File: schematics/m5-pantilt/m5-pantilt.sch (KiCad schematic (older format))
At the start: 11 parts, among them J1 Conn_02x15_Odd_Even, J2 Conn_02x03_Odd_Even, J3 Conn_02x03_Odd_Even, J4 Conn_02x03_Odd_Even, J5 BAT, J6 Conn_01x04, SW1 SW_SPDT, U1 NL27WZ125

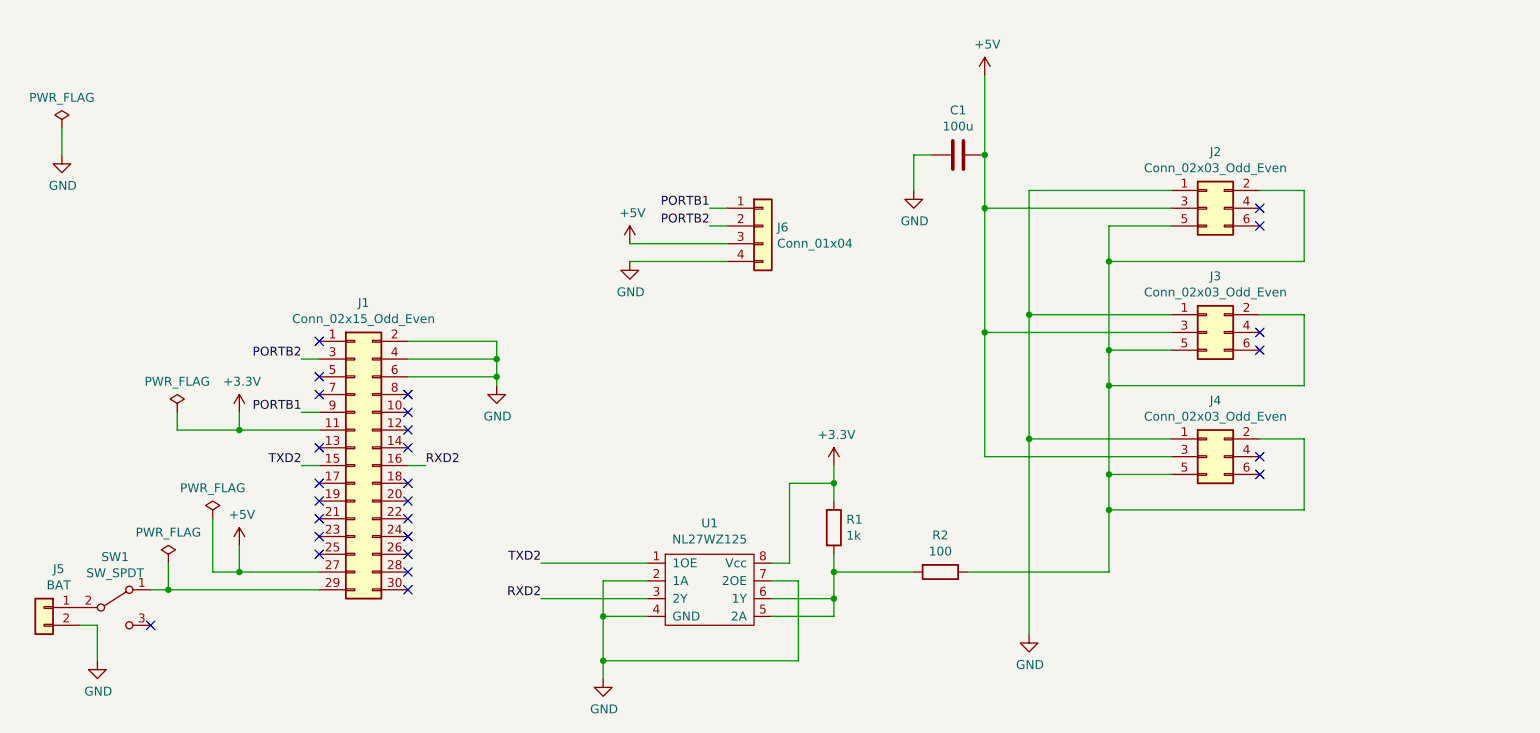
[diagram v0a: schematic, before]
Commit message: Make schematics and layout
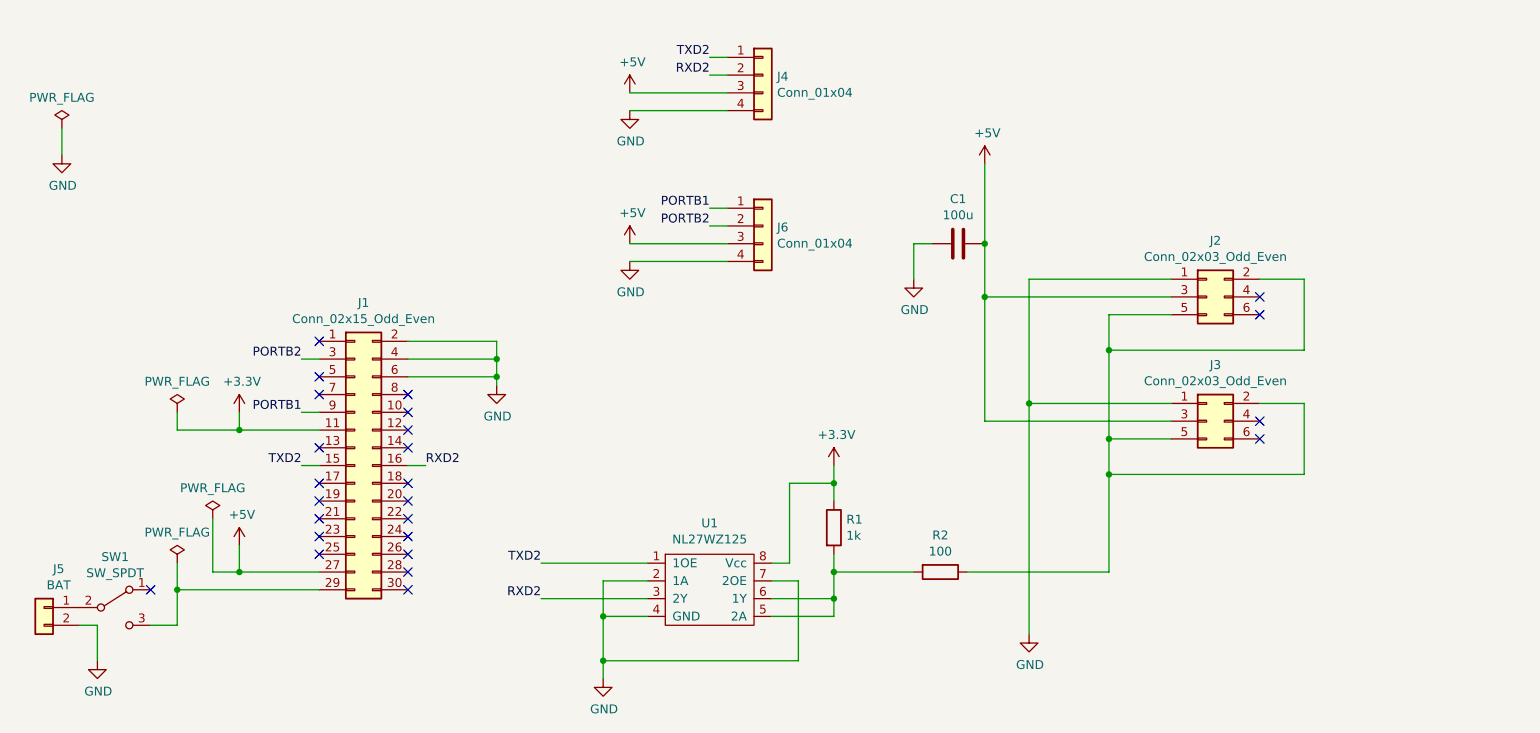
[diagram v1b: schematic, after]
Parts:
- removed J4: Conn_02x03_Odd_Even, Connector_PinHeader_2.54mm:PinHeader_2x03_P2.54mm_Vertical, symbol Connector_Generic:Conn_02x03_Odd_Even
- added J4: Conn_01x04, Connector_JST:JST_PH_S4B-PH-K_1x04_P2.00mm_Horizontal, symbol Connector_Generic:Conn_01x04
- J1: footprint Connector_PinHeader_2.54mm:PinHeader_2x15_P2.54mm_Vertical -> Connector_PinHeader_2.54mm:PinHeader_2x15_P2.54mm_Vertical_SMD
- SW1: footprint Button_Switch_THT:SW_CuK_OS102011MA1QN1_SPDT_Angled -> Button_Switch_THT:SW_E-Switch_EG1224_SPDT_Angled
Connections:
- net +5V: now also J4.3 (Pin_3)
- net GND: now also J4.4 (Pin_4)
- net RXD2: now also J4.2 (Pin_2)
- net TXD2: now also J4.1 (Pin_1)
- net at J1.29 (Pin_29): now also SW1.3 (C); no longer SW1.1 (A)
- no-connect marks 27 -> 25
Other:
- moved on the sheet: C1, J2, J3
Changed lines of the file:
@@
 F 0 "J1" H 3800 5467 50  0000 C CNN
 F 1 "Conn_02x15_Odd_Even" H 3800 5376 50  0000 C CNN
-F 2 "Connector_PinHeader_2.54mm:PinHeader_2x15_P2.54mm_Vertical" H 3750 4550 50  0001 C CNN
+F 2 "Connector_PinHeader_2.54mm:PinHeader_2x15_P2.54mm_Vertical_SMD" H 3750 4550 50  0001 C CNN
 F 3 "~" H 3750 4550 50  0001 C CNN
 	1    3750 4550
@@
 L Connector_Generic:Conn_02x03_Odd_Even J3
 U 1 1 60BD706E
-P 8550 3800
-F 0 "J3" H 8600 4117 50  0000 C CNN
-F 1 "Conn_02x03_Odd_Even" H 8600 4026 50  0000 C CNN
-F 2 "Connector_PinHeader_2.54mm:PinHeader_2x03_P2.54mm_Vertical" H 8550 3800 50  0001 C CNN
-F 3 "~" H 8550 3800 50  0001 C CNN
-	1    8550 3800
-	1    0    0    -1
-$EndComp
-$Comp
-L Connector_Generic:Conn_02x03_Odd_Even J4
-U 1 1 60BD7329
-P 8550 4500
-F 0 "J4" H 8600 4817 50  0000 C CNN
-F 1 "Conn_02x03_Odd_Even" H 8600 4726 50  0000 C CNN
-F 2 "Connector_PinHeader_2.54mm:PinHeader_2x03_P2.54mm_Vertical" H 8550 4500 50  0001 C CNN
-F 3 "~" H 8550 4500 50  0001 C CNN
-	1    8550 4500
+P 8550 4300
+F 0 "J3" H 8600 4617 50  0000 C CNN
+F 1 "Conn_02x03_Odd_Even" H 8600 4526 50  0000 C CNN
+F 2 "Connector_PinHeader_2.54mm:PinHeader_2x03_P2.54mm_Vertical" H 8550 4300 50  0001 C CNN
+F 3 "~" H 8550 4300 50  0001 C CNN
+	1    8550 4300
 	1    0    0    -1
 $EndComp
@@
 L power:+5V #PWR07
 U 1 1 60BFD6E8
-P 7300 2350
-F 0 "#PWR07" H 7300 2200 50  0001 C CNN
-F 1 "+5V" H 7315 2523 50  0000 C CNN
-F 2 "" H 7300 2350 50  0001 C CNN
-F 3 "" H 7300 2350 50  0001 C CNN
-	1    7300 2350
+P 7300 2850
+F 0 "#PWR07" H 7300 2700 50  0001 C CNN
+F 1 "+5V" H 7315 3023 50  0000 C CNN
+F 2 "" H 7300 2850 50  0001 C CNN
+F 3 "" H 7300 2850 50  0001 C CNN
+	1    7300 2850
 	1    0    0    -1
 $EndComp
@@
 	7200 5150 8000 5150
 Wire Wire Line
-	8000 4600 8350 4600
+	8000 4400 8350 4400
+Wire Wire Line
+	8000 4400 8000 4600
+Wire Wire Line
+	8000 4600 9100 4600
+Wire Wire Line
+	9100 4600 9100 4200
+Wire Wire Line
+	9100 4200 8850 4200
 Connection ~ 8000 4600
 Wire Wire Line
-	8000 4600 8000 4800
-Wire Wire Line
-	8000 3900 8350 3900
-Wire Wire Line
-	8000 3900 8000 4100
-Wire Wire Line
-	8000 4100 9100 4100
-Wire Wire Line
-	9100 4100 9100 3700
-Wire Wire Line
-	9100 3700 8850 3700
-Connection ~ 8000 4100
-Wire Wire Line
-	8000 4100 8000 4600
-Wire Wire Line
-	8850 4400 9100 4400
-Wire Wire Line
-	9100 4400 9100 4800
-Wire Wire Line
-	9100 4800 8000 4800
-Connection ~ 8000 4800
-Wire Wire Line
-	8000 4800 8000 5150
-Wire Wire Line
-	7300 3800 8350 3800
-Wire Wire Line
-	7300 2350 7300 2800
-Wire Wire Line
-	7300 3800 7300 4500
-Wire Wire Line
-	7300 4500 8350 4500
-Connection ~ 7300 3800
-NoConn ~ 8850 4500
-NoConn ~ 8850 3800
-NoConn ~ 8850 3900
-NoConn ~ 8850 4600
-Wire Wire Line
-	7550 5500 7550 4400
-Wire Wire Line
-	7550 4400 8350 4400
-Wire Wire Line
-	7550 4400 7550 3700
-Wire Wire Line
-	7550 3700 8350 3700
-Connection ~ 7550 4400
+	7300 4300 8350 4300
+Wire Wire Line
+	7300 2850 7300 3300
+NoConn ~ 8850 4300
+NoConn ~ 8850 4400
+Wire Wire Line
+	7550 4200 8350 4200
 $Comp
 L Connector_Generic:Conn_02x03_Odd_Even J2
 U 1 1 60C1A998
-P 8550 3100
-F 0 "J2" H 8600 3417 50  0000 C CNN
-F 1 "Conn_02x03_Odd_Even" H 8600 3326 50  0000 C CNN
-F 2 "Connector_PinHeader_2.54mm:PinHeader_2x03_P2.54mm_Vertical" H 8550 3100 50  0001 C CNN
-F 3 "~" H 8550 3100 50  0001 C CNN
-	1    8550 3100
-	1    0    0    -1
-$EndComp
-Wire Wire Line
-	8000 3200 8350 3200
-Wire Wire Line
-	8000 3400 9100 3400
-Wire Wire Line
-	7300 3100 8350 3100
-Wire Wire Line
-	7550 3000 8350 3000
-Wire Wire Line
-	8850 3000 9100 3000
-Wire Wire Line
-	9100 3000 9100 3400
-NoConn ~ 8850 3100
-NoConn ~ 8850 3200
-Wire Wire Line
-	8000 3200 8000 3400
-Wire Wire Line
-	8000 3400 8000 3900
-Connection ~ 8000 3400
+P 8550 3600
+F 0 "J2" H 8600 3917 50  0000 C CNN
+F 1 "Conn_02x03_Odd_Even" H 8600 3826 50  0000 C CNN
+F 2 "Connector_PinHeader_2.54mm:PinHeader_2x03_P2.54mm_Vertical" H 8550 3600 50  0001 C CNN
+F 3 "~" H 8550 3600 50  0001 C CNN
+	1    8550 3600
+	1    0    0    -1
+$EndComp
+Wire Wire Line
+	8000 3700 8350 3700
+Wire Wire Line
+	8000 3900 9100 3900
+Wire Wire Line
+	7300 3600 8350 3600
+Wire Wire Line
+	7550 3500 8350 3500
+Wire Wire Line
+	8850 3500 9100 3500
+Wire Wire Line
+	9100 3500 9100 3900
+NoConn ~ 8850 3600
+NoConn ~ 8850 3700
+Wire Wire Line
+	8000 3700 8000 3900
+Wire Wire Line
+	8000 3900 8000 4400
 Connection ~ 8000 3900
-Connection ~ 7300 3100
-Wire Wire Line
-	7300 3100 7300 3800
-Wire Wire Line
-	7550 3000 7550 3700
-Connection ~ 7550 3700
+Connection ~ 8000 4400
+Connection ~ 7300 3600
+Wire Wire Line
+	7300 3600 7300 4300
+Wire Wire Line
+	7550 3500 7550 4200
+Connection ~ 7550 4200
 Text Label 3450 3950 2    50   ~ 0
 PORTB2
@@
 L power:PWR_FLAG #FLG0101
 U 1 1 60C7066B
-P 2700 5100
-F 0 "#FLG0101" H 2700 5175 50  0001 C CNN
-F 1 "PWR_FLAG" H 2700 5273 50  0000 C CNN
-F 2 "" H 2700 5100 50  0001 C CNN
-F 3 "~" H 2700 5100 50  0001 C CNN
-	1    2700 5100
+P 2750 5100
+F 0 "#FLG0101" H 2750 5175 50  0001 C CNN
+F 1 "PWR_FLAG" H 2750 5273 50  0000 C CNN
+F 2 "" H 2750 5100 50  0001 C CNN
+F 3 "~" H 2750 5100 50  0001 C CNN
+	1    2750 5100
 	1    0    0    -1
 $EndComp
@@
 Wire Wire Line
 	5300 3400 5850 3400
-Connection ~ 7300 2800
-Wire Wire Line
-	7300 2800 7300 3100
+Connection ~ 7300 3300
+Wire Wire Line
+	7300 3300 7300 3600
 $Comp
 L power:GND #PWR0101
 U 1 1 60CBA560
-P 6900 3000
-F 0 "#PWR0101" H 6900 2750 50  0001 C CNN
-F 1 "GND" H 6905 2827 50  0000 C CNN
-F 2 "" H 6900 3000 50  0001 C CNN
-F 3 "" H 6900 3000 50  0001 C CNN
-	1    6900 3000
-	1    0    0    -1
-$EndComp
-Wire Wire Line
-	6900 3000 6900 2800
-Wire Wire Line
-	6900 2800 7000 2800
+P 6900 3500
+F 0 "#PWR0101" H 6900 3250 50  0001 C CNN
+F 1 "GND" H 6905 3327 50  0000 C CNN
+F 2 "" H 6900 3500 50  0001 C CNN
+F 3 "" H 6900 3500 50  0001 C CNN
+	1    6900 3500
+	1    0    0    -1
+$EndComp
+Wire Wire Line
+	6900 3500 6900 3300
+Wire Wire Line
+	6900 3300 7000 3300
 $Comp
 L Device:C C1
 U 1 1 60CB98BD
-P 7150 2800
-F 0 "C1" V 7402 2800 50  0000 C CNN
-F 1 "100u" V 7311 2800 50  0000 C CNN
-F 2 "Capacitor_THT:C_Radial_D6.3mm_H11.0mm_P2.50mm" H 7188 2650 50  0001 C CNN
-F 3 "~" H 7150 2800 50  0001 C CNN
-	1    7150 2800
+P 7150 3300
+F 0 "C1" V 7402 3300 50  0000 C CNN
+F 1 "100u" V 7311 3300 50  0000 C CNN
+F 2 "Capacitor_THT:C_Radial_D6.3mm_H11.0mm_P2.50mm" H 7188 3150 50  0001 C CNN
+F 3 "~" H 7150 3300 50  0001 C CNN
+	1    7150 3300
 	0    -1   -1   0
 $EndComp
@@
 F 0 "SW1" H 2400 5635 50  0000 C CNN
 F 1 "SW_SPDT" H 2400 5544 50  0000 C CNN
-F 2 "Button_Switch_THT:SW_CuK_OS102011MA1QN1_SPDT_Angled" H 2400 5350 50  0001 C CNN
+F 2 "Button_Switch_THT:SW_E-Switch_EG1224_SPDT_Angled" H 2400 5350 50  0001 C CNN
 F 3 "~" H 2400 5350 50  0001 C CNN
 	1    2400 5350
@@
 $EndComp
 Wire Wire Line
-	2600 5250 2700 5250
-Wire Wire Line
 	2200 5450 2300 5450
 Wire Wire Line
 	2300 5450 2300 5650
-NoConn ~ 2600 5450
-Wire Wire Line
-	2700 5100 2700 5250
-Connection ~ 2700 5250
-Wire Wire Line
-	2700 5250 3550 5250
+Wire Wire Line
+	2750 5100 2750 5250
+Wire Wire Line
+	2750 5250 3550 5250
 $Comp
 L power:PWR_FLAG #FLG0105
@@
 Wire Wire Line
 	2100 2650 2100 2800
+Wire Wire Line
+	8000 4600 8000 5150
+Wire Wire Line
+	7550 4200 7550 5500
+NoConn ~ 2600 5250
+Wire Wire Line
+	2750 5250 2750 5450
+Wire Wire Line
+	2750 5450 2600 5450
+Connection ~ 2750 5250
+$Comp
+L Connector_Generic:Conn_01x04 J4
+U 1 1 60C5F21C
+P 6050 2350
+F 0 "J4" H 6130 2342 50  0000 L CNN
+F 1 "Conn_01x04" H 6130 2251 50  0000 L CNN
+F 2 "Connector_JST:JST_PH_S4B-PH-K_1x04_P2.00mm_Horizontal" H 6050 2350 50  0001 C CNN
+F 3 "~" H 6050 2350 50  0001 C CNN
+	1    6050 2350
+	1    0    0    -1
+$EndComp
+Wire Wire Line
+	5750 2250 5850 2250
+Wire Wire Line
+	5750 2350 5850 2350
+$Comp
+L power:+5V #PWR01
+U 1 1 60C5F226
+P 5300 2450
+F 0 "#PWR01" H 5300 2300 50  0001 C CNN
+F 1 "+5V" H 5315 2623 50  0000 C CNN
+F 2 "" H 5300 2450 50  0001 C CNN
+F 3 "" H 5300 2450 50  0001 C CNN
+	1    5300 2450
+	1    0    0    -1
+$EndComp
+Wire Wire Line
+	5300 2450 5850 2450
+$Comp
+L power:GND #PWR011
+U 1 1 60C5F22D
+P 5300 2550
+F 0 "#PWR011" H 5300 2300 50  0001 C CNN
+F 1 "GND" H 5305 2377 50  0000 C CNN
+F 2 "" H 5300 2550 50  0001 C CNN
+F 3 "" H 5300 2550 50  0001 C CNN
+	1    5300 2550
+	1    0    0    -1
+$EndComp
+Wire Wire Line
+	5300 2550 5850 2550
+Text Label 5750 2350 2    50   ~ 0
+RXD2
+Text Label 5750 2250 2    50   ~ 0
+TXD2
 $EndSCHEMATC
